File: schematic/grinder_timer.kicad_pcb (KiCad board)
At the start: 2 copper layers, 75 x 120 mm, 31 parts, among them J1 AVR-ISP-6, J2 SERIAL, K1 Relay, P1 MOTOR, P2 ACTIVE, P3 NEUTRAL, Q1 NPN, T1 1P1S, U1 ATmega328PB-AU, U2 5V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

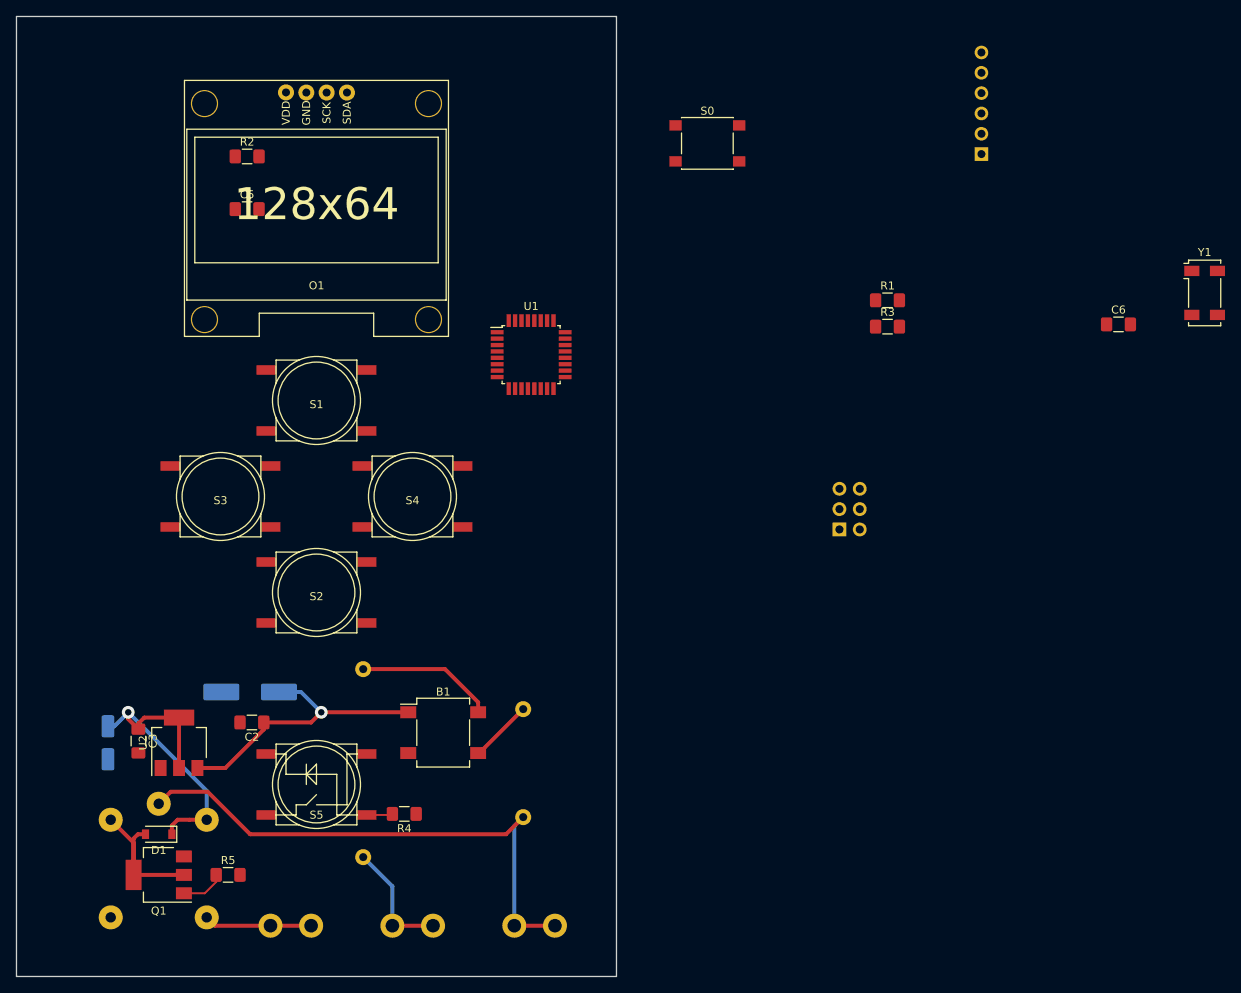
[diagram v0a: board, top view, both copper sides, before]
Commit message: Switched transformer.  Completed PCB layout.  Added silkscreen logos.
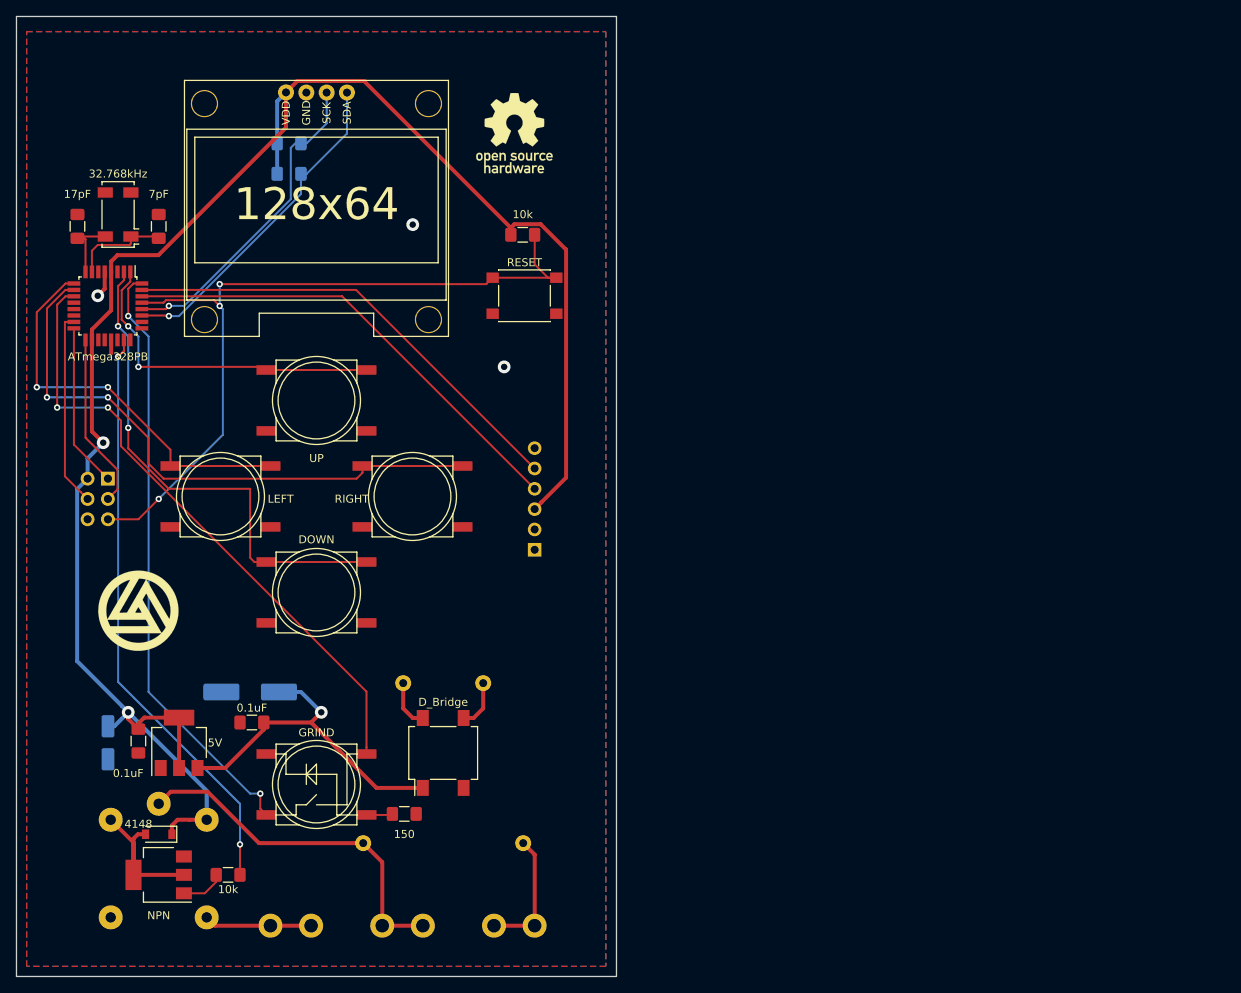
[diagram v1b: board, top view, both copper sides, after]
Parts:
- added G***: LOGO, grinder_timer:oshw_logo_10mm, B.Cu at (37.5, -91.4)
- added G***: LOGO, grinder_timer:oshw_logo_10mm, F.Cu at (62.2, -105.4)
- added G***: LOGO, grinder_timer:clews_logo_10mm, F.Cu at (15.2, -45.7)
- added G***: LOGO, grinder_timer:clews_logo_30mm, B.Cu at (37.5, -60.0)
- J2: footprint Connector_PinHeader_2.54mm:PinHeader_1x06_P2.54mm_Horizontal -> Connector_PinHeader_2.54mm:PinHeader_1x06_P2.54mm_Vertical
- R1, R2: moved to B.Cu
- T1: footprint grinder_timer:transformer -> grinder_timer:transformer_big
- U1: value ATmega328PB-AU -> ATmega328PB
- moved Y1 136.2 mm to (12.7, -95.2), turned to 180 degrees
- moved C6 130.7 mm to (7.62, -93.8), turned to 270 degrees
- moved J1 91.7 mm to (11.4, -62.2), turned to 180 degrees
- moved R1 76.5 mm to (34.1, -100.3)
- moved J2 74.6 mm to (64.8, -53.3)
- moved U1 53.2 mm to (11.4, -83.8), turned to 270 degrees
- moved R3 47.0 mm to (63.3, -92.7)
- moved S0 29.8 mm to (63.5, -85.1), turned to 180 degrees
- moved P2 16.5 mm to (48.3, -6.35)
- moved P3 12.7 mm to (62.2, -6.35)
- moved C5 11.3 mm to (17.8, -93.8), turned to 270 degrees
- moved R2 5.49 mm to (34.1, -104.1)
- moved B1 2.54 mm to (53.3, -27.9), turned to 90 degrees
- turned T1 to 0 degrees
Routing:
- net +5V: track 41.5 -> 226.9 mm, vias 1 -> 2
- net !RST: track 0.00 -> 97.4 mm, vias 0 -> 3
- net Net-(S5-Pad1): track 0.00 -> 78.4 mm, vias 0 -> 2
- net Net-(S5-Pad4): track 0.00 -> 75.7 mm, vias 0 -> 2
- net Net-(S4-Pad1): track 0.00 -> 74.6 mm, vias 0 -> 2
- net RELAY: track 0.00 -> 73.5 mm, vias 0 -> 2
- net Net-(S2-Pad1): track 0.00 -> 63.6 mm, vias 0 -> 2
- net AVR_RX: track 0.00 -> 59.1 mm
- net AVR_TX: track 0.00 -> 58.3 mm
- net Net-(S3-Pad1): track 0.00 -> 50.0 mm, vias 0 -> 2
- net Net-(S1-Pad1): track 0.00 -> 41.9 mm, vias 0 -> 2
- net SDA: track 0.00 -> 41.7 mm, vias 0 -> 1
- net SCL: track 0.00 -> 40.3 mm, vias 0 -> 1
- net MOSI: track 0.00 -> 24.4 mm
- net Net-(K1-Pad11): track 68.4 -> 45.2 mm
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- added copper zone on B.Cu, net GND
- added copper zone on F.Cu, net GND
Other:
- net class Power: clearance 0.4 -> 0.2
- board text added: "!DTR RX (AVR_TX) TX (AVR_RX) VCC !CTS GND"
- board text added: "https://clews.pro"

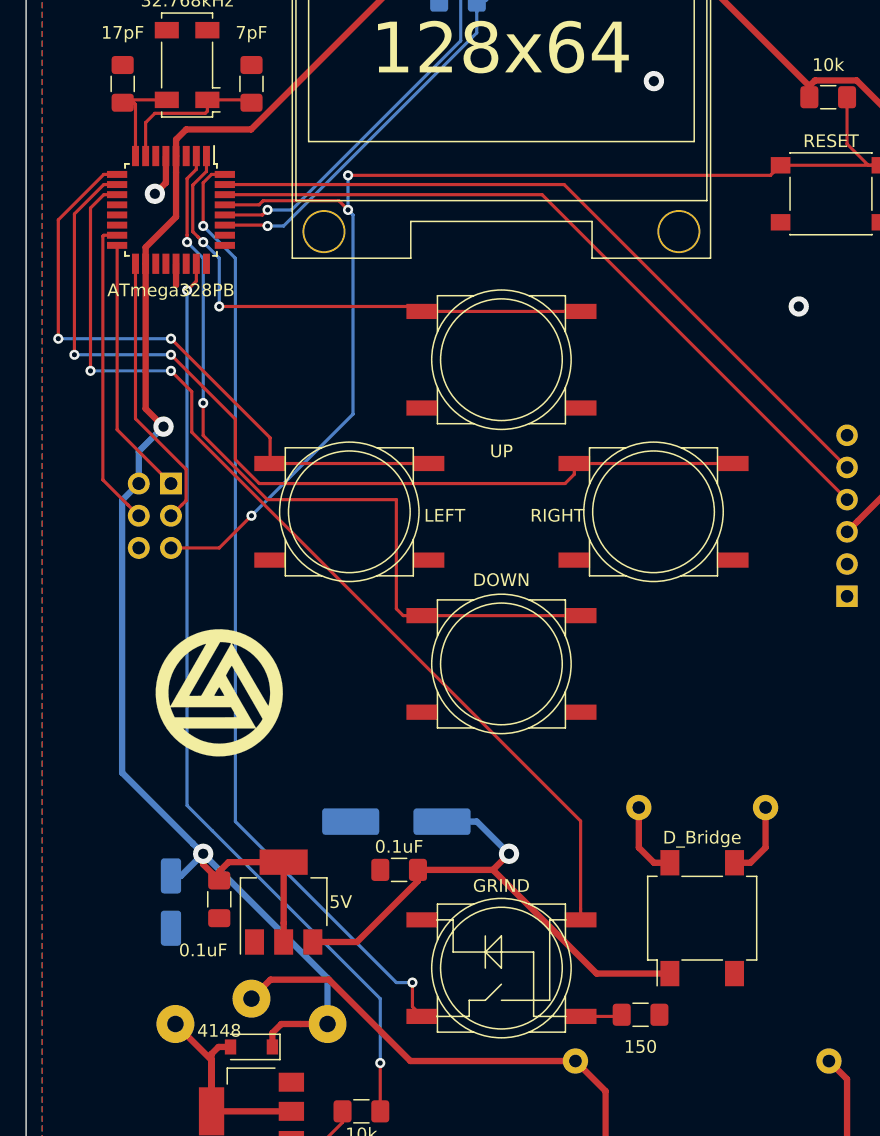
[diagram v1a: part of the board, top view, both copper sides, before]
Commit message: Fixed let tact switch pinout.  Modified via sizes.
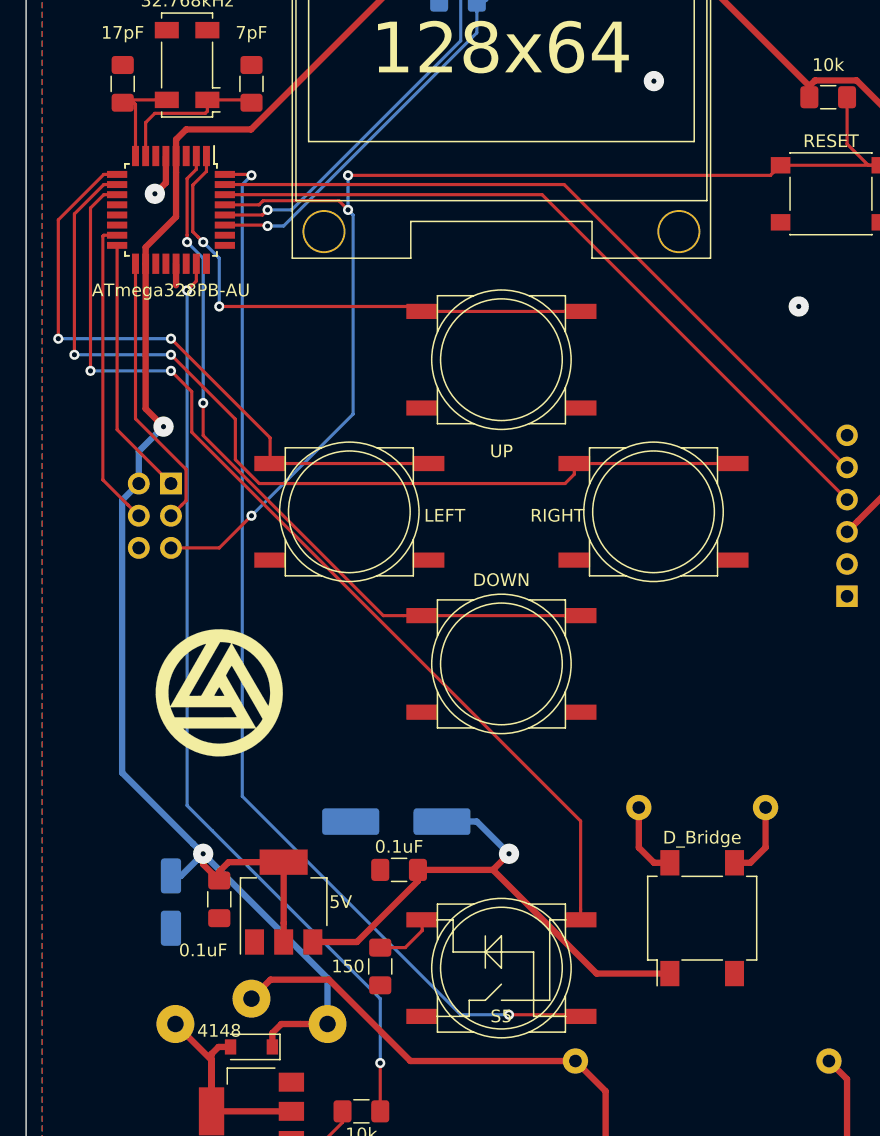
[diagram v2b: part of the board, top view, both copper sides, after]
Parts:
- U1: value ATmega328PB -> ATmega328PB-AU
- moved R4 20.9 mm to (27.9, -24.1), turned to 90 degrees
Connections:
- S5 pad 2: GND -> Net-(R4-Pad2)
- S5 pad 3: Net-(R4-Pad2) -> Net-(S5-Pad3)
- S5 pad 4: Net-(S5-Pad4) -> GND
- U1 pad 32: Net-(S5-Pad4) -> Net-(S5-Pad3)
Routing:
- net Net-(S5-Pad3): track 0.00 -> 85.3 mm, vias 0 -> 2
- net Net-(S5-Pad4): track 75.7 -> 0.00 mm, vias 2 -> 0
- net Net-(S2-Pad1): track 63.6 -> 58.5 mm
- net Net-(R4-Pad2): track 3.29 -> 4.72 mm
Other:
- net class Power: via_drill 0.8 -> 0.4

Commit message: I2C pull-up values were too high, changed from 10k to 3.3k.
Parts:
- R1, R2: value 10k -> 3.3k
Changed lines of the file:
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@@
       (effects (font (size 1 1) (thickness 0.15)) (justify mirror))
     )
-    (fp_text value 10k (at -3.5925 0) (layer B.SilkS)
+    (fp_text value 3.3k (at -3.8465 0) (layer B.SilkS)
       (effects (font (size 1 1) (thickness 0.15)) (justify mirror))
     )
@@
       (effects (font (size 1 1) (thickness 0.15)) (justify mirror))
     )
-    (fp_text value 10k (at -3.5925 0) (layer B.SilkS)
+    (fp_text value 3.3k (at -3.8465 0) (layer B.SilkS)
       (effects (font (size 1 1) (thickness 0.15)) (justify mirror))
     )
